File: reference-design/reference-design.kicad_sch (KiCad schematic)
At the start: 21 parts

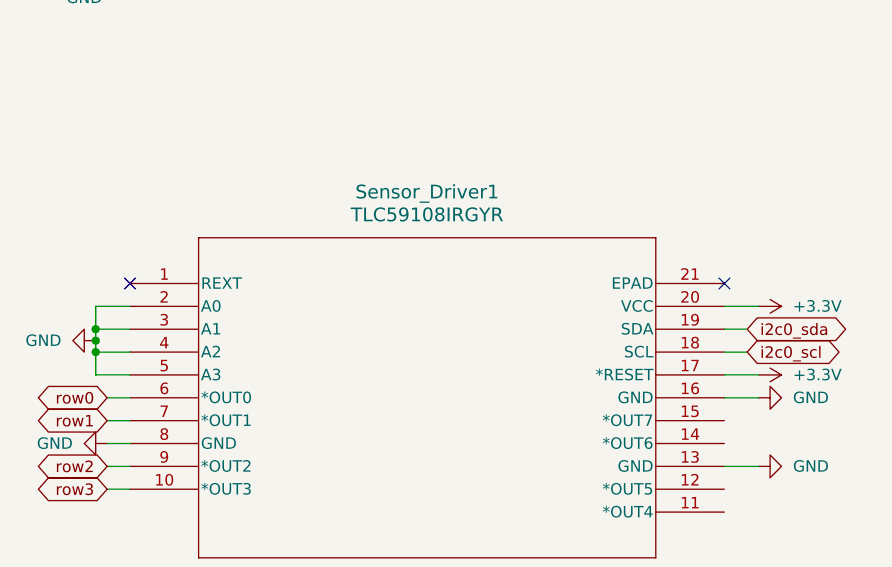
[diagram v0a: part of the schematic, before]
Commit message: associate 3d models for pcb preview
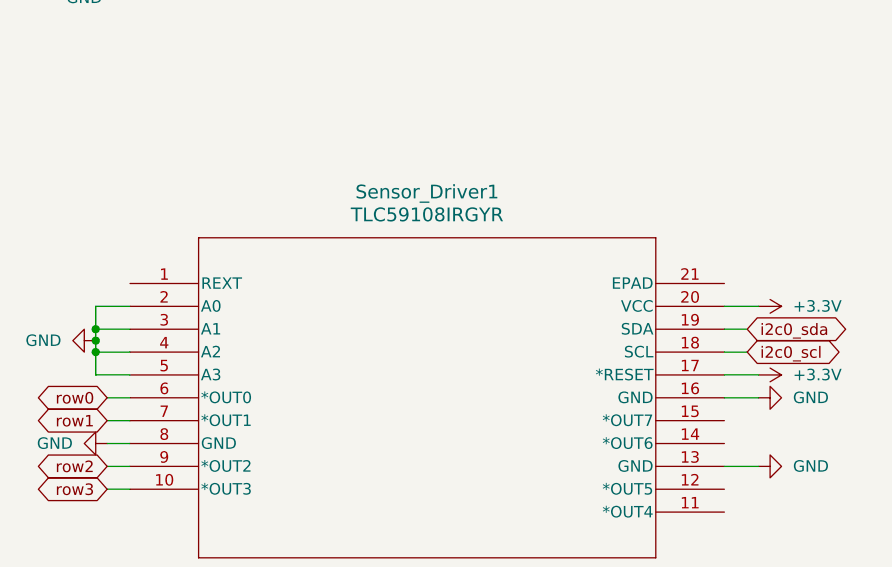
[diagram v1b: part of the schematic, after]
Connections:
- no-connect marks 2 -> 0
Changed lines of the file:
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@@
 		(color 0 0 0 0)
-	)
-	(no_connect
-		(at 26.67 152.4)
-	)
-	(no_connect
-		(at 92.71 152.4)
 	)
 	(wire

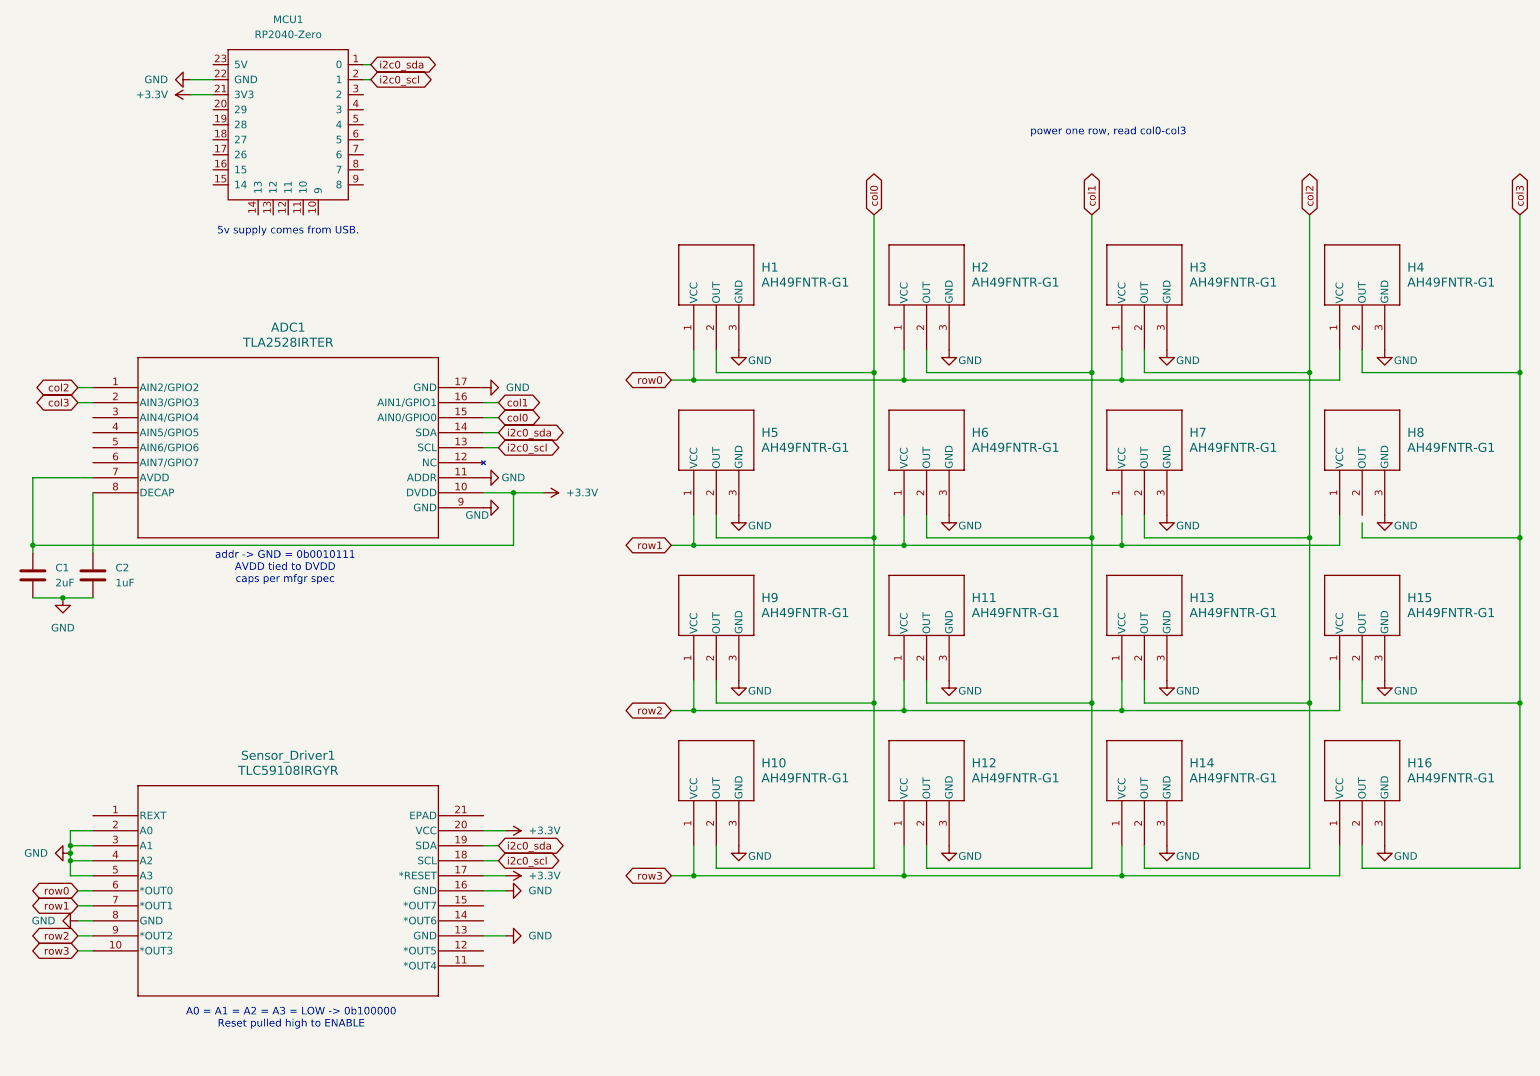
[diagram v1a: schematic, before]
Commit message: SCH and PCB cleanup
- Ran ERC
- Added NCs to unused pins
- Fixed unconnected output pin on one of the sensors
- Cleaned up expected violations
- Rearranged sensors on PCB to match the pattern on the schematic
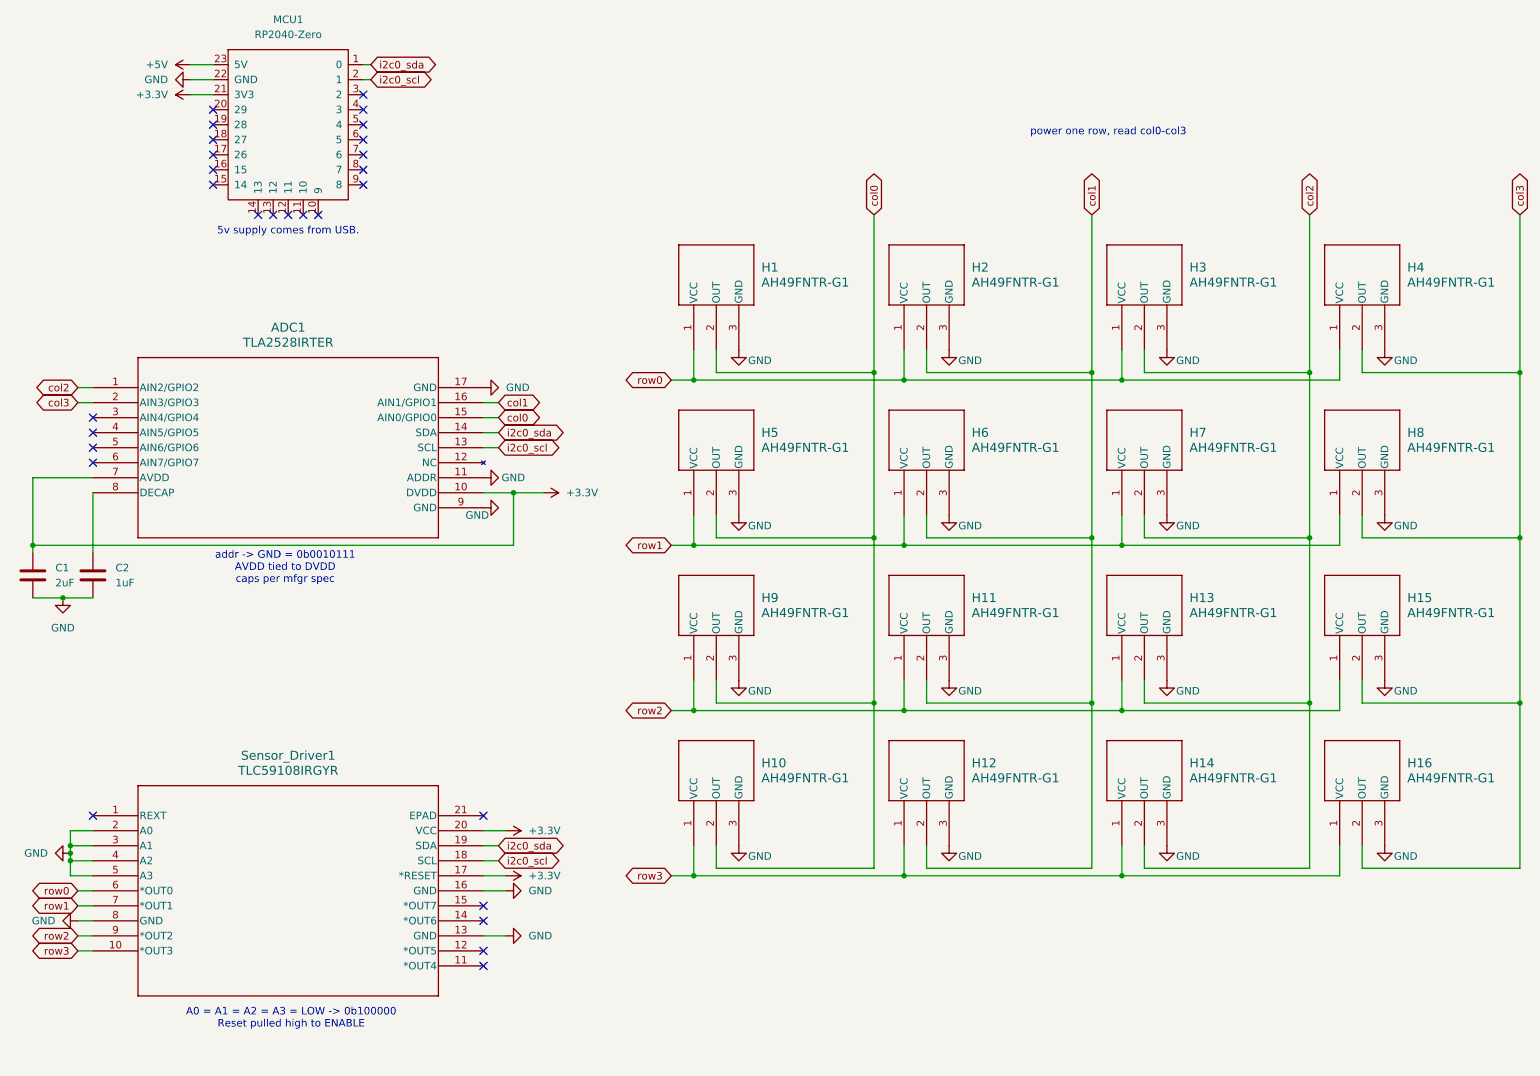
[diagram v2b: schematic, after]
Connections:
- net col3: now also H8.2 (OUT)
- net +5V: now reaches MCU1.23 (5V)
- no-connect marks 0 -> 28
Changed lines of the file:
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@@
 		(color 0 0 0 0)
 	)
+	(no_connect
+		(at 72.39 35.56)
+	)
+	(no_connect
+		(at 72.39 45.72)
+	)
+	(no_connect
+		(at 46.99 43.18)
+	)
+	(no_connect
+		(at 72.39 40.64)
+	)
+	(no_connect
+		(at 46.99 33.02)
+	)
+	(no_connect
+		(at 72.39 38.1)
+	)
+	(no_connect
+		(at 92.71 177.8)
+	)
+	(no_connect
+		(at 64.77 50.8)
+	)
+	(no_connect
+		(at 62.23 50.8)
+	)
+	(no_connect
+		(at 26.67 85.09)
+	)
+	(no_connect
+		(at 72.39 30.48)
+	)
+	(no_connect
+		(at 26.67 92.71)
+	)
+	(no_connect
+		(at 54.61 50.8)
+	)
+	(no_connect
+		(at 92.71 167.64)
+	)
+	(no_connect
+		(at 72.39 33.02)
+	)
+	(no_connect
+		(at 26.67 152.4)
+	)
+	(no_connect
+		(at 72.39 43.18)
+	)
+	(no_connect
+		(at 92.71 175.26)
+	)
+	(no_connect
+		(at 59.69 50.8)
+	)
+	(no_connect
+		(at 46.99 35.56)
+	)
+	(no_connect
+		(at 26.67 90.17)
+	)
+	(no_connect
+		(at 46.99 40.64)
+	)
+	(no_connect
+		(at 46.99 38.1)
+	)
+	(no_connect
+		(at 26.67 87.63)
+	)
+	(no_connect
+		(at 92.71 170.18)
+	)
+	(no_connect
+		(at 57.15 50.8)
+	)
+	(no_connect
+		(at 46.99 45.72)
+	)
+	(no_connect
+		(at 92.71 152.4)
+	)
 	(wire
 		(pts
@@
 	(wire
 		(pts
-			(xy 241.3 102.87) (xy 241.3 105.41)
+			(xy 241.3 101.6) (xy 241.3 105.41)
 		)
 		(stroke
@@
 		(pts
 			(xy 163.83 162.56) (xy 200.66 162.56)
+		)
+		(stroke
+			(width 0)
+			(type default)
+		)
+	)
+	(wire
+		(pts
+			(xy 43.18 25.4) (xy 46.99 25.4)
 		)
 		(stroke
@@
 					(unit 1)
 				)
+			)
+		)
+	)
+	(symbol
+		(lib_id "power:+3.3V")
+		(at 43.18 25.4 90)
+		(unit 1)
+		(exclude_from_sim no)
+		(in_bom yes)
+		(on_board yes)
+		(dnp no)
+		(fields_autoplaced yes)
+		(property "Reference" "#PWR030"
+			(at 46.99 25.4 0)
+			(effects
+				(font
+					(size 1.27 1.27)
+				)
+				(hide yes)
+			)
+		)
+		(property "Value" "+5V"
+			(at 39.37 25.3999 90)
+			(effects
+				(font
+					(size 1.27 1.27)
+				)
+				(justify left)
+			)
+		)
+		(property "Footprint" ""
+			(at 43.18 25.4 0)
+			(effects
+				(font
+					(size 1.27 1.27)
+				)
+				(hide yes)
+			)
+		)
+		(property "Datasheet" ""
+			(at 43.18 25.4 0)
+			(effects
+				(font
+					(size 1.27 1.27)
+				)
+				(hide yes)
+			)
+		)
+		(property "Description" "Power symbol creates a global label with name \"+3.3V\""
+			(at 43.18 25.4 0)
+			(effects
+				(font
+					(size 1.27 1.27)
+				)
+				(hide yes)
+			)
+		)
+		(pin "1"
+		)
+		(instances
+			(project "reference-design"
+				(path "/1bb90a40-7122-4522-9655-ffb2519dec46"
+					(reference "#PWR030")
+					(unit 1)
+				)

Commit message: Re-commit
Last commit had improperly saved files.
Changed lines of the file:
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@@
+	)
+	(junction
+		(at 267.97 105.41)
+		(diameter 0)
+		(color 0 0 0 0)
 	)
 	(junction
@@
 		(color 0 0 0 0)
 	)
-	(junction
-		(at 267.97 105.41)
-		(diameter 0)
-		(color 0 0 0 0)
-	)
 	(no_connect
 		(at 72.39 35.56)
@@
 	(wire
 		(pts
-			(xy 267.97 105.41) (xy 267.97 77.47)
+			(xy 237.49 101.6) (xy 237.49 106.68)
 		)
 		(stroke
@@
 	(wire
 		(pts
-			(xy 237.49 106.68) (xy 237.49 101.6)
-		)
-		(stroke
-			(width 0)
-			(type default)
-		)
-	)
-	(wire
-		(pts
 			(xy 73.66 25.4) (xy 72.39 25.4)
 		)
@@
 	(wire
 		(pts
-			(xy 267.97 133.35) (xy 267.97 105.41)
-		)
-		(stroke
-			(width 0)
-			(type default)
-		)
-	)
-	(wire
-		(pts
 			(xy 97.79 106.68) (xy 16.51 106.68)
 		)
@@
 	(wire
 		(pts
+			(xy 267.97 105.41) (xy 267.97 133.35)
+		)
+		(stroke
+			(width 0)
+			(type default)
+		)
+	)
+	(wire
+		(pts
 			(xy 158.75 77.47) (xy 132.08 77.47)
 		)
@@
 	(wire
 		(pts
+			(xy 267.97 77.47) (xy 267.97 105.41)
+		)
+		(stroke
+			(width 0)
+			(type default)
+		)
+	)
+	(wire
+		(pts
 			(xy 232.41 133.35) (xy 204.47 133.35)
 		)
@@
 	(wire
 		(pts
+			(xy 241.3 101.6) (xy 241.3 105.41)
+		)
+		(stroke
+			(width 0)
+			(type default)
+		)
+	)
+	(wire
+		(pts
 			(xy 22.86 162.56) (xy 26.67 162.56)
 		)
@@
 		)
 		(stroke
-			(width 0)
-			(type default)
-		)
-	)
-	(wire
-		(pts
-			(xy 241.3 101.6) (xy 241.3 105.41)
-		)
-		(stroke
